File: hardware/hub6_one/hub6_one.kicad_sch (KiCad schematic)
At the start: 10 parts, among them J1 plate 1, J2 plate 2, J3 plate 3, J4 plate 4, J5 plate 5, J6 base, U1 74HC138, U2 XIAO ESP32S3

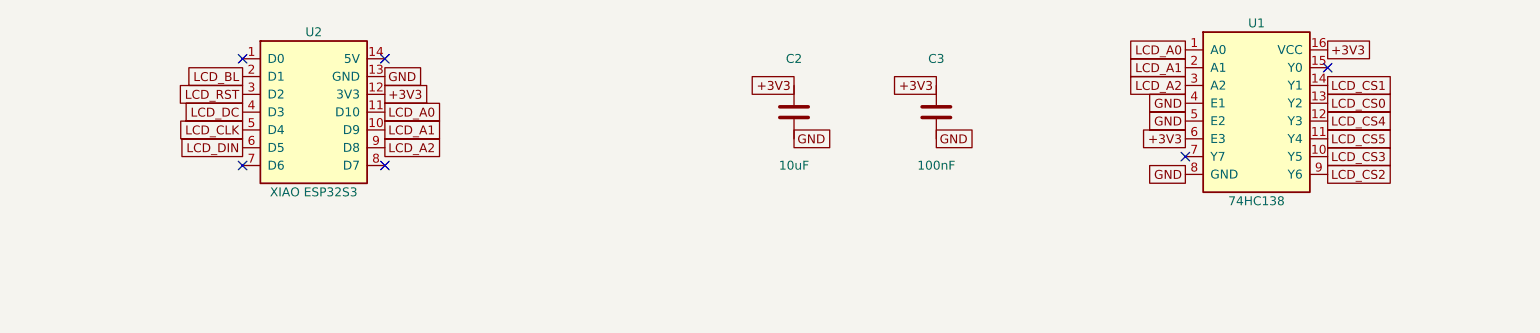
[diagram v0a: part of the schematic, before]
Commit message: hub6_one: the XIAO in two female sockets under the board, parts as hub3's
The XIAO now plugs into two 1x7 8.5 mm female sockets (C2832270) on the underside,
3 mm off the middle toward 342 degrees so that, hanging lower, it clears the base
display's plug: with the connectors as they are (top entry, 3 mm proud of the plate,
the plug 2 mm more; tmp/connectors.py) nothing touches, 1.5 mm to the nearest. Plate 3's
chip select goes round the chip's USB-C end now (Y0); P1 Y2, P2 Y1, P3 Y0, P4 Y5, P5 Y3,
base Y4. U1 is C2674688, as on cubic-earth's hub3 (the capacitors and sockets were
already the same). fab.py writes the sockets as bottom-side parts. ERC, DRC, parity clean.

Claude-Session: https://claude.ai/code/session_01WVeYczw2dnncq6csD58pZW
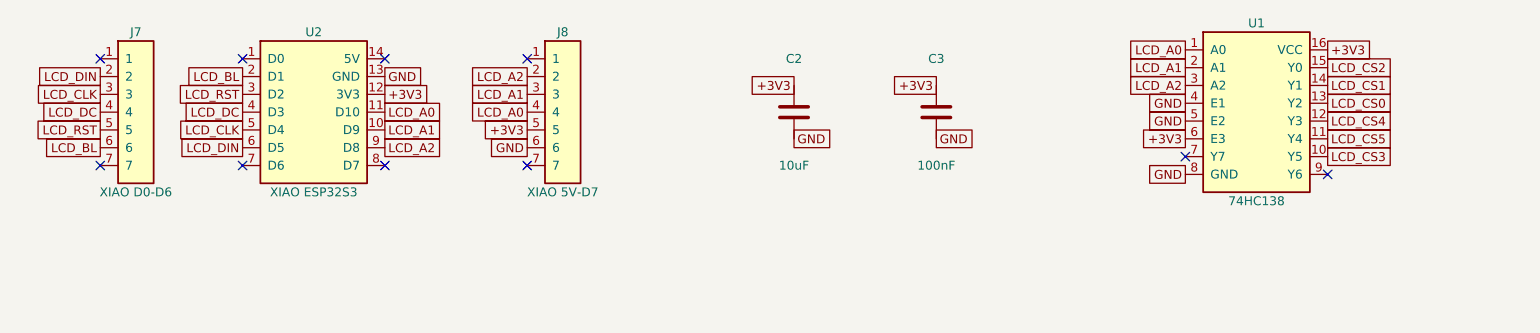
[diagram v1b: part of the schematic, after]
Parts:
- added J7: XIAO D0-D6, Connector_PinSocket_2.54mm:PinSocket_1x07_P2.54mm_Vertical, symbol dodecahedron-earth:Socket_1x07
- added J8: XIAO 5V-D7, Connector_PinSocket_2.54mm:PinSocket_1x07_P2.54mm_Vertical, symbol dodecahedron-earth:Socket_1x07
- U1: LCSC C5602 -> C2674688
- U2: footprint dodecahedron-earth:XIAO_ESP32S3_Hanging -> (none)
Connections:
- net +3V3: now also J8.5
- net GND: now also J8.6
- net LCD_A0: now also J8.4
- net LCD_A1: now also J8.3
- net LCD_A2: now also J8.2
- net LCD_BL: now also J7.6
- net LCD_CLK: now also J7.3
- net LCD_CS2: now also U1.15 (Y0); no longer U1.9 (Y6)
- net LCD_DC: now also J7.4
- net LCD_DIN: now also J7.2
- net LCD_RST: now also J7.5
- no-connect marks 6 -> 10

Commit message: hub6_one: the XIAO's sockets are soldered by hand, out of the BOM and CPL
J7 and J8 keep their footprints (the same C2832270 as hub3's, noted in fab6/README.md for
buying) and are excluded from the BOM and the placement file: JLCPCB places only U1, C2
and C3, all on top. ERC, DRC, parity clean.

Claude-Session: https://claude.ai/code/session_01WVeYczw2dnncq6csD58pZW
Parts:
- J7, J8: LCSC C2832270 -> (none); now left out of the parts list
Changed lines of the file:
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@@
 (pin "7")
 (pin "8")
-(instances (project "hub6_one" (path "/9b4c247e-2df4-49b2-a298-d2eb3e85fe6b" (reference "J1") (unit 1)))))
+(instances (project "hub6_one" (path "/6076395b-bc6e-41c2-833f-7235c4420dfb" (reference "J1") (unit 1)))))
 (global_label "+3V3" (shape passive) (at 25.40 140.97 180) (effects (font (size 1.27 1.27)) (justify right)))
 (global_label "GND" (shape passive) (at 25.40 143.51 180) (effects (font (size 1.27 1.27)) (justify right)))
@@
 (pin "7")
 (pin "8")
-(instances (project "hub6_one" (path "/9b4c247e-2df4-49b2-a298-d2eb3e85fe6b" (reference "J2") (unit 1)))))
+(instances (project "hub6_one" (path "/6076395b-bc6e-41c2-833f-7235c4420dfb" (reference "J2") (unit 1)))))
 (global_label "+3V3" (shape passive) (at 71.12 140.97 180) (effects (font (size 1.27 1.27)) (justify right)))
 (global_label "GND" (shape passive) (at 71.12 143.51 180) (effects (font (size 1.27 1.27)) (justify right)))
@@
 (pin "7")
 (pin "8")
-(instances (project "hub6_one" (path "/9b4c247e-2df4-49b2-a298-d2eb3e85fe6b" (reference "J3") (unit 1)))))
+(instances (project "hub6_one" (path "/6076395b-bc6e-41c2-833f-7235c4420dfb" (reference "J3") (unit 1)))))
 (global_label "+3V3" (shape passive) (at 114.30 140.97 180) (effects (font (size 1.27 1.27)) (justify right)))
 (global_label "GND" (shape passive) (at 114.30 143.51 180) (effects (font (size 1.27 1.27)) (justify right)))
@@
 (pin "7")
 (pin "8")
-(instances (project "hub6_one" (path "/9b4c247e-2df4-49b2-a298-d2eb3e85fe6b" (reference "J4") (unit 1)))))
+(instances (project "hub6_one" (path "/6076395b-bc6e-41c2-833f-7235c4420dfb" (reference "J4") (unit 1)))))
 (global_label "+3V3" (shape passive) (at 160.02 140.97 180) (effects (font (size 1.27 1.27)) (justify right)))
 (global_label "GND" (shape passive) (at 160.02 143.51 180) (effects (font (size 1.27 1.27)) (justify right)))
@@
 (pin "7")
 (pin "8")
-(instances (project "hub6_one" (path "/9b4c247e-2df4-49b2-a298-d2eb3e85fe6b" (reference "J5") (unit 1)))))
+(instances (project "hub6_one" (path "/6076395b-bc6e-41c2-833f-7235c4420dfb" (reference "J5") (unit 1)))))
 (global_label "+3V3" (shape passive) (at 205.74 140.97 180) (effects (font (size 1.27 1.27)) (justify right)))
 (global_label "GND" (shape passive) (at 205.74 143.51 180) (effects (font (size 1.27 1.27)) (justify right)))
@@
 (pin "7")
 (pin "8")
-(instances (project "hub6_one" (path "/9b4c247e-2df4-49b2-a298-d2eb3e85fe6b" (reference "J6") (unit 1)))))
+(instances (project "hub6_one" (path "/6076395b-bc6e-41c2-833f-7235c4420dfb" (reference "J6") (unit 1)))))
 (global_label "+3V3" (shape passive) (at 248.92 140.97 180) (effects (font (size 1.27 1.27)) (justify right)))
 (global_label "GND" (shape passive) (at 248.92 143.51 180) (effects (font (size 1.27 1.27)) (justify right)))
@@
 (pin "9")
 (pin "8")
-(instances (project "hub6_one" (path "/9b4c247e-2df4-49b2-a298-d2eb3e85fe6b" (reference "U2") (unit 1)))))
+(instances (project "hub6_one" (path "/6076395b-bc6e-41c2-833f-7235c4420dfb" (reference "U2") (unit 1)))))
 (no_connect (at 30.48 63.50))
 (global_label "LCD_BL" (shape passive) (at 30.48 66.04 180) (effects (font (size 1.27 1.27)) (justify right)))
@@
 (global_label "LCD_A2" (shape passive) (at 50.80 76.20 0) (effects (font (size 1.27 1.27)) (justify left)))
 (no_connect (at 50.80 78.74))
-(symbol (lib_id "dodecahedron-earth:Socket_1x07") (at 15.24 71.12 0) (unit 1) (exclude_from_sim no) (in_bom yes) (on_board yes) (dnp no)
+(symbol (lib_id "dodecahedron-earth:Socket_1x07") (at 15.24 71.12 0) (unit 1) (exclude_from_sim no) (in_bom no) (on_board yes) (dnp no)
 (property "Reference" "J7" (at 15.24 59.69 0) (effects (font (size 1.27 1.27))))
 (property "Value" "XIAO D0-D6" (at 15.24 82.55 0) (effects (font (size 1.27 1.27))))
 (property "Footprint" "Connector_PinSocket_2.54mm:PinSocket_1x07_P2.54mm_Vertical" (at 15.24 71.12 0) (effects (font (size 1.27 1.27)) hide))
 (property "Datasheet" "" (at 15.24 71.12 0) (effects (font (size 1.27 1.27)) hide))
-(property "LCSC" "C2832270" (at 15.24 71.12 0) (effects (font (size 1.27 1.27)) hide))
-(pin "1")
-(pin "2")
-(pin "3")
-(pin "4")
-(pin "5")
-(pin "6")
-(pin "7")
-(instances (project "hub6_one" (path "/9b4c247e-2df4-49b2-a298-d2eb3e85fe6b" (reference "J7") (unit 1)))))
+(pin "1")
+(pin "2")
+(pin "3")
+(pin "4")
+(pin "5")
+(pin "6")
+(pin "7")
+(instances (project "hub6_one" (path "/6076395b-bc6e-41c2-833f-7235c4420dfb" (reference "J7") (unit 1)))))
 (no_connect (at 10.16 63.50))
 (global_label "LCD_DIN" (shape passive) (at 10.16 66.04 180) (effects (font (size 1.27 1.27)) (justify right)))
@@
 (global_label "LCD_BL" (shape passive) (at 10.16 76.20 180) (effects (font (size 1.27 1.27)) (justify right)))
 (no_connect (at 10.16 78.74))
-(symbol (lib_id "dodecahedron-earth:Socket_1x07") (at 76.20 71.12 0) (unit 1) (exclude_from_sim no) (in_bom yes) (on_board yes) (dnp no)
+(symbol (lib_id "dodecahedron-earth:Socket_1x07") (at 76.20 71.12 0) (unit 1) (exclude_from_sim no) (in_bom no) (on_board yes) (dnp no)
 (property "Reference" "J8" (at 76.20 59.69 0) (effects (font (size 1.27 1.27))))
 (property "Value" "XIAO 5V-D7" (at 76.20 82.55 0) (effects (font (size 1.27 1.27))))
 (property "Footprint" "Connector_PinSocket_2.54mm:PinSocket_1x07_P2.54mm_Vertical" (at 76.20 71.12 0) (effects (font (size 1.27 1.27)) hide))
 (property "Datasheet" "" (at 76.20 71.12 0) (effects (font (size 1.27 1.27)) hide))
-(property "LCSC" "C2832270" (at 76.20 71.12 0) (effects (font (size 1.27 1.27)) hide))
-(pin "1")
-(pin "2")
-(pin "3")
-(pin "4")
-(pin "5")
-(pin "6")
-(pin "7")
-(instances (project "hub6_one" (path "/9b4c247e-2df4-49b2-a298-d2eb3e85fe6b" (reference "J8") (unit 1)))))
+(pin "1")
+(pin "2")
+(pin "3")
+(pin "4")
+(pin "5")
+(pin "6")
+(pin "7")
+(instances (project "hub6_one" (path "/6076395b-bc6e-41c2-833f-7235c4420dfb" (reference "J8") (unit 1)))))
 (no_connect (at 71.12 63.50))
 (global_label "LCD_A2" (shape passive) (at 71.12 66.04 180) (effects (font (size 1.27 1.27)) (justify right)))
@@
 (pin "10")
 (pin "9")
-(instances (project "hub6_one" (path "/9b4c247e-2df4-49b2-a298-d2eb3e85fe6b" (reference "U1") (unit 1)))))
+(instances (project "hub6_one" (path "/6076395b-bc6e-41c2-833f-7235c4420dfb" (reference "U1") (unit 1)))))
 (global_label "LCD_A0" (shape passive) (at 165.10 62.23 180) (effects (font (size 1.27 1.27)) (justify right)))
 (global_label "LCD_A1" (shape passive) (at 165.10 64.77 180) (effects (font (size 1.27 1.27)) (justify right)))
@@
 (pin "1")
 (pin "2")
-(instances (project "hub6_one" (path "/9b4c247e-2df4-49b2-a298-d2eb3e85fe6b" (reference "C2") (unit 1)))))
+(instances (project "hub6_one" (path "/6076395b-bc6e-41c2-833f-7235c4420dfb" (reference "C2") (unit 1)))))
 (global_label "+3V3" (shape passive) (at 109.22 67.31 180) (effects (font (size 1.27 1.27)) (justify right)))
 (global_label "GND" (shape passive) (at 109.22 74.93 0) (effects (font (size 1.27 1.27)) (justify left)))
@@
 (pin "1")
 (pin "2")
-(instances (project "hub6_one" (path "/9b4c247e-2df4-49b2-a298-d2eb3e85fe6b" (reference "C3") (unit 1)))))
+(instances (project "hub6_one" (path "/6076395b-bc6e-41c2-833f-7235c4420dfb" (reference "C3") (unit 1)))))
 (global_label "+3V3" (shape passive) (at 129.54 67.31 180) (effects (font (size 1.27 1.27)) (justify right)))
 (global_label "GND" (shape passive) (at 129.54 74.93 0) (effects (font (size 1.27 1.27)) (justify left)))
